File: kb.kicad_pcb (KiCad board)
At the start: 2 copper layers, 203.2 x 114.3 mm, 186 parts, among them J1 Conn_02x04, J2 10029449-001RLF, J3 Conn_01x05, J4 Conn_01x10, J5 Conn_01x07, J6 Conn_01x06, SW1 RotaryEncoder_Switch, U1 Pico, U2 SN74AHCT125D

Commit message: Add signature :)
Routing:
- net GND: vias 174 -> 173
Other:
- board text added: "GND---|----5V"
- board text added: "Split Keyboard Left rev. 1 Designed by Jiayi Tang in Edmonton, Alberta, Canada July 2022"
- board text removed: "5V----|---GND"

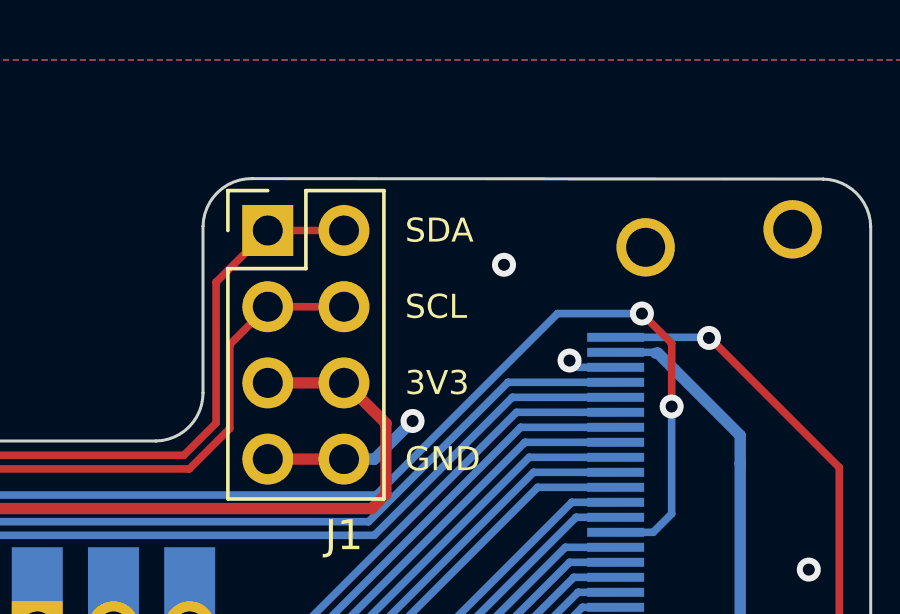
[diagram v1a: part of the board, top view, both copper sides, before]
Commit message: Add pullup i2c
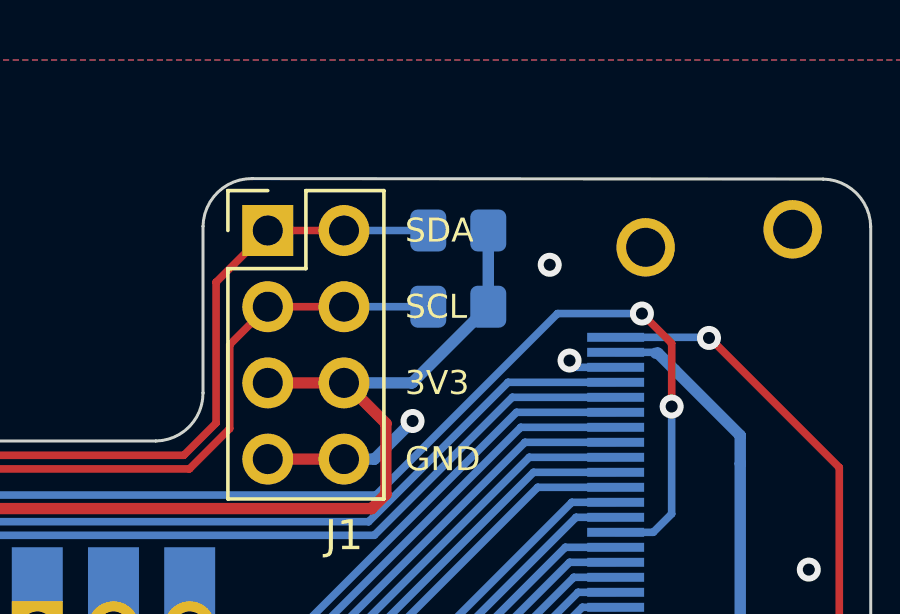
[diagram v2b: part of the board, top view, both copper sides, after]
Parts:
- added R1: R_Small_US, Resistor_SMD:R_0805_2012Metric_Pad1.20x1.40mm_HandSolder, B.Cu at (95.0, 44.6)
- added R2: R_Small_US, Resistor_SMD:R_0805_2012Metric_Pad1.20x1.40mm_HandSolder, B.Cu at (95.0, 47.1)
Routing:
- net +3V3: track 66.8 -> 75.2 mm
- net /OLED_SDA: track 48.9 -> 51.7 mm
- net /OLED_SCL: track 44.2 -> 47.0 mm
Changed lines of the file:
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@@
     )
   )
+  (footprint "Resistor_SMD:R_0805_2012Metric_Pad1.20x1.40mm_HandSolder" (layer "B.Cu")
+    (at 94.996 44.577 180)
+    (descr "Resistor SMD 0805 (2012 Metric), square (rectangular) end terminal, IPC_7351 nominal with elongated pad for handsoldering. (Body size source: IPC-SM-782 page 72, https://www.pcb-3d.com/wordpress/wp-content/uploads/ipc-sm-782a_amendment_1_and_2.pdf), generated with kicad-footprint-generator")
+    (tags "resistor handsolder")
+    (property "Sheetfile" "kb.kicad_sch")
+    (property "Sheetname" "")
+    (attr smd)
+    (fp_text reference "R1" (at -2.921 0) (layer "B.SilkS")
+      (effects (font (size 1 1) (thickness 0.15)) (justify mirror))
+    )
+    (fp_text value "R_Small_US" (at 0 -1.65) (layer "B.Fab")
+      (effects (font (size 1 1) (thickness 0.15)) (justify mirror))
+    )
+    (fp_text user "${REFERENCE}" (at 0 0) (layer "B.Fab")
+      (effects (font (size 0.5 0.5) (thickness 0.08)) (justify mirror))
+    )
+    (fp_line (start -0.227064 -0.735) (end 0.227064 -0.735) (layer "B.SilkS") (width 0.12))
+    (fp_line (start -0.227064 0.735) (end 0.227064 0.735) (layer "B.SilkS") (width 0.12))
+    (fp_line (start 1.85 -0.95) (end -1.85 -0.95) (layer "B.CrtYd") (width 0.05))
+    (fp_line (start 1.85 0.95) (end 1.85 -0.95) (layer "B.CrtYd") (width 0.05))
+    (fp_line (start -1.85 -0.95) (end -1.85 0.95) (layer "B.CrtYd") (width 0.05))
+    (fp_line (start -1.85 0.95) (end 1.85 0.95) (layer "B.CrtYd") (width 0.05))
+    (fp_line (start 1 0.625) (end 1 -0.625) (layer "B.Fab") (width 0.1))
+    (fp_line (start 1 -0.625) (end -1 -0.625) (layer "B.Fab") (width 0.1))
+    (fp_line (start -1 0.625) (end 1 0.625) (layer "B.Fab") (width 0.1))
+    (fp_line (start -1 -0.625) (end -1 0.625) (layer "B.Fab") (width 0.1))
+    (pad "1" smd roundrect (at -1 0 180) (size 1.2 1.4) (layers "B.Cu" "B.Paste" "B.Mask") (roundrect_rratio 0.208333)
+      (net 76 "+3V3") (pintype "passive"))
+    (pad "2" smd roundrect (at 1 0 180) (size 1.2 1.4) (layers "B.Cu" "B.Paste" "B.Mask") (roundrect_rratio 0.208333)
+      (net 9 "/OLED_SDA") (pintype "passive"))
+    (model "${KICAD6_3DMODEL_DIR}/Resistor_SMD.3dshapes/R_0805_2012Metric.wrl"
+      (offset (xyz 0 0 0))
+      (scale (xyz 1 1 1))
+      (rotate (xyz 0 0 0))
+    )
+  )
   (footprint "Capacitor_SMD:C_0805_2012Metric_Pad1.18x1.45mm_HandSolder" (layer "B.Cu")
     (at 93.6625 76.99375 90)
@@
     )
   )
+  (footprint "Resistor_SMD:R_0805_2012Metric_Pad1.20x1.40mm_HandSolder" (layer "B.Cu")
+    (at 94.996 47.117 180)
+    (descr "Resistor SMD 0805 (2012 Metric), square (rectangular) end terminal, IPC_7351 nominal with elongated pad for handsoldering. (Body size source: IPC-SM-782 page 72, https://www.pcb-3d.com/wordpress/wp-content/uploads/ipc-sm-782a_amendment_1_and_2.pdf), generated with kicad-footprint-generator")
+    (tags "resistor handsolder")
+    (property "Sheetfile" "kb.kicad_sch")
+    (property "Sheetname" "")
+    (attr smd)
+    (fp_text reference "R2" (at -2.921 0) (layer "B.SilkS")
+      (effects (font (size 1 1) (thickness 0.15)) (justify mirror))
+    )
+    (fp_text value "R_Small_US" (at 0 -1.65) (layer "B.Fab")
+      (effects (font (size 1 1) (thickness 0.15)) (justify mirror))
+    )
+    (fp_text user "${REFERENCE}" (at 0 0) (layer "B.Fab")
+      (effects (font (size 0.5 0.5) (thickness 0.08)) (justify mirror))
+    )
+    (fp_line (start -0.227064 -0.735) (end 0.227064 -0.735) (layer "B.SilkS") (width 0.12))
+    (fp_line (start -0.227064 0.735) (end 0.227064 0.735) (layer "B.SilkS") (width 0.12))
+    (fp_line (start 1.85 0.95) (end 1.85 -0.95) (layer "B.CrtYd") (width 0.05))
+    (fp_line (start -1.85 0.95) (end 1.85 0.95) (layer "B.CrtYd") (width 0.05))
+    (fp_line (start 1.85 -0.95) (end -1.85 -0.95) (layer "B.CrtYd") (width 0.05))
+    (fp_line (start -1.85 -0.95) (end -1.85 0.95) (layer "B.CrtYd") (width 0.05))
+    (fp_line (start 1 0.625) (end 1 -0.625) (layer "B.Fab") (width 0.1))
+    (fp_line (start -1 0.625) (end 1 0.625) (layer "B.Fab") (width 0.1))
+    (fp_line (start -1 -0.625) (end -1 0.625) (layer "B.Fab") (width 0.1))
+    (fp_line (start 1 -0.625) (end -1 -0.625) (layer "B.Fab") (width 0.1))
+    (pad "1" smd roundrect (at -1 0 180) (size 1.2 1.4) (layers "B.Cu" "B.Paste" "B.Mask") (roundrect_rratio 0.208333)
+      (net 76 "+3V3") (pintype "passive"))
+    (pad "2" smd roundrect (at 1 0 180) (size 1.2 1.4) (layers "B.Cu" "B.Paste" "B.Mask") (roundrect_rratio 0.208333)
+      (net 8 "/OLED_SCL") (pintype "passive"))
+    (model "${KICAD6_3DMODEL_DIR}/Resistor_SMD.3dshapes/R_0805_2012Metric.wrl"
+      (offset (xyz 0 0 0))
+      (scale (xyz 1 1 1))
+      (rotate (xyz 0 0 0))
+    )
+  )
   (footprint "Keebio-Parts:SK6812-MINI-E" (layer "B.Cu")
     (at 37.30625 96.04375 180)
@@
     (property "Sheetname" "")
     (attr through_hole)
-    (fp_text reference "J2" (at -7.8105 3.32375 180) (layer "B.SilkS")
+    (fp_text reference "J2" (at 9.9695 0.02175 180) (layer "B.SilkS")
       (effects (font (size 1 1) (thickness 0.15)) (justify mirror))
     )
@@
   (via (at 53.467 118.364) (size 0.8) (drill 0.4) (layers "F.Cu" "B.Cu") (free) (net 2))
   (via (at 121.92 127) (size 0.8) (drill 0.4) (layers "F.Cu" "B.Cu") (free) (net 2))
-  (via (at 96.52 45.72) (size 0.8) (drill 0.4) (layers "F.Cu" "B.Cu") (free) (net 2))
+  (via (at 98.044 45.72) (size 0.8) (drill 0.4) (layers "F.Cu" "B.Cu") (free) (net 2))
   (via (at 128.524 141.605) (size 0.8) (drill 0.4) (layers "F.Cu" "B.Cu") (free) (net 2))
   (via (at 177.8 91.44) (size 0.8) (drill 0.4) (layers "F.Cu" "B.Cu") (free) (net 2))
@@
   (segment (start 87.376 48.387) (end 88.646 47.117) (width 0.254) (layer "F.Cu") (net 8))
   (segment (start 58.28398 52.52352) (end 86.03348 52.52352) (width 0.254) (layer "F.Cu") (net 8))
+  (segment (start 93.996 47.117) (end 91.186 47.117) (width 0.254) (layer "B.Cu") (net 8))
   (segment (start 88.646 44.577) (end 91.186 44.577) (width 0.254) (layer "F.Cu") (net 9))
   (segment (start 86.92248 46.30052) (end 88.646 44.577) (width 0.254) (layer "F.Cu") (net 9))
@@
   (segment (start 85.845626 52.07) (end 86.92248 50.993146) (width 0.254) (layer "F.Cu") (net 9))
   (segment (start 86.92248 50.993146) (end 86.92248 46.30052) (width 0.254) (layer "F.Cu") (net 9))
+  (segment (start 93.996 44.577) (end 91.186 44.577) (width 0.254) (layer "B.Cu") (net 9))
   (segment (start 46.482 142.494) (end 46.482 144.613169) (width 0.254) (layer "F.Cu") (net 10))
   (segment (start 47.371 124.206) (end 46.482 123.317) (width 0.254) (layer "F.Cu") (net 10))
@@
   (segment (start 64.422511 58.29863) (end 64.422511 57.331348) (width 0.381) (layer "F.Cu") (net 76))
   (segment (start 67.905859 53.848) (end 92.107022 53.848) (width 0.381) (layer "F.Cu") (net 76))
+  (segment (start 93.456 49.657) (end 95.996 47.117) (width 0.381) (layer "B.Cu") (net 76))
+  (segment (start 91.186 49.657) (end 93.456 49.657) (width 0.381) (layer "B.Cu") (net 76))
+  (segment (start 95.996 47.117) (end 95.996 44.577) (width 0.381) (layer "B.Cu") (net 76))
   (segment (start 92.007772 54.28348) (end 96.653752 49.6375) (width 0.254) (layer "B.Cu") (net 77))
   (segment (start 62.530998 54.28348) (end 92.007772 54.28348) (width 0.254) (layer "B.Cu") (net 77))
